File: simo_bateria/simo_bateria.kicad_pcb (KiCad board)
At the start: 2 copper layers, 40.5 x 90 mm, 7 parts, among them J1 Conn_01x02_Male, J2 Conn_01x02_Male, U1 conversor_dc_1_1

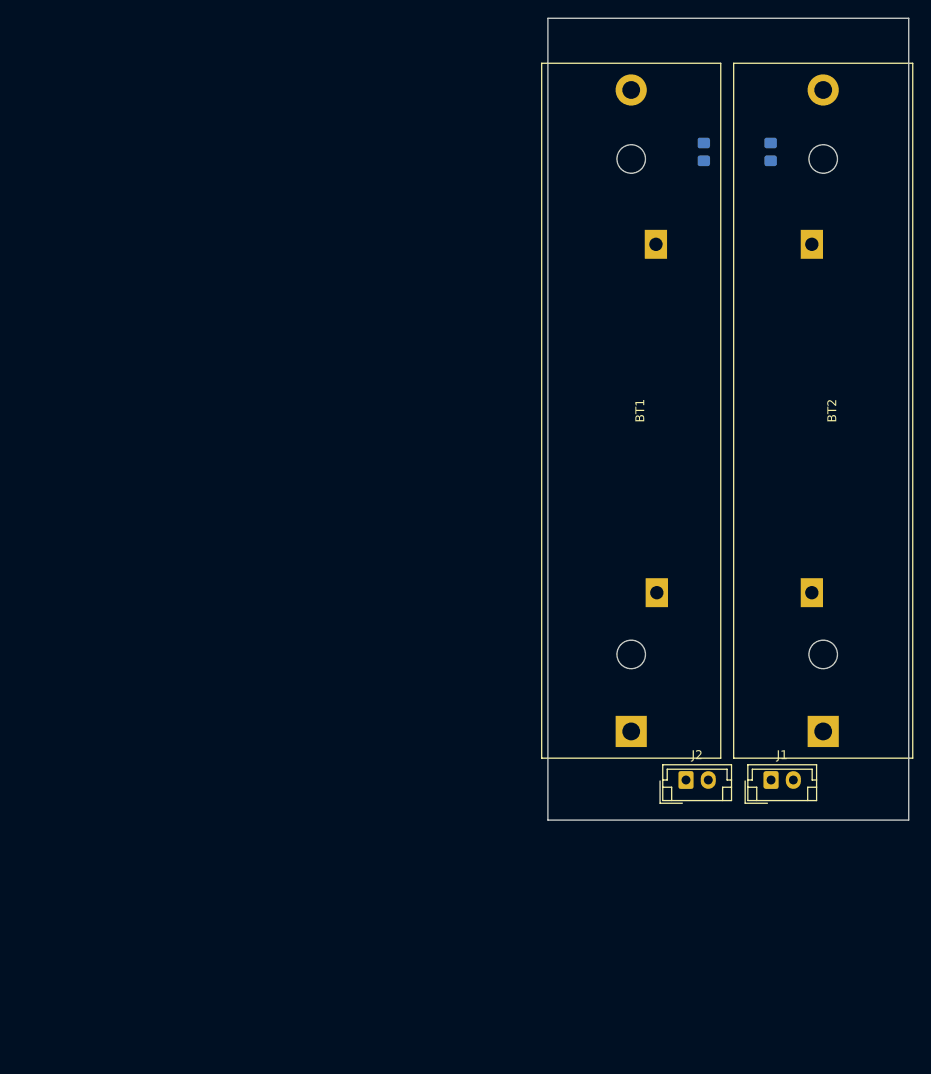
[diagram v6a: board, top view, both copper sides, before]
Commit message: update: placa bateria, correccion de error en esquematico:GND de la salida LEVEL
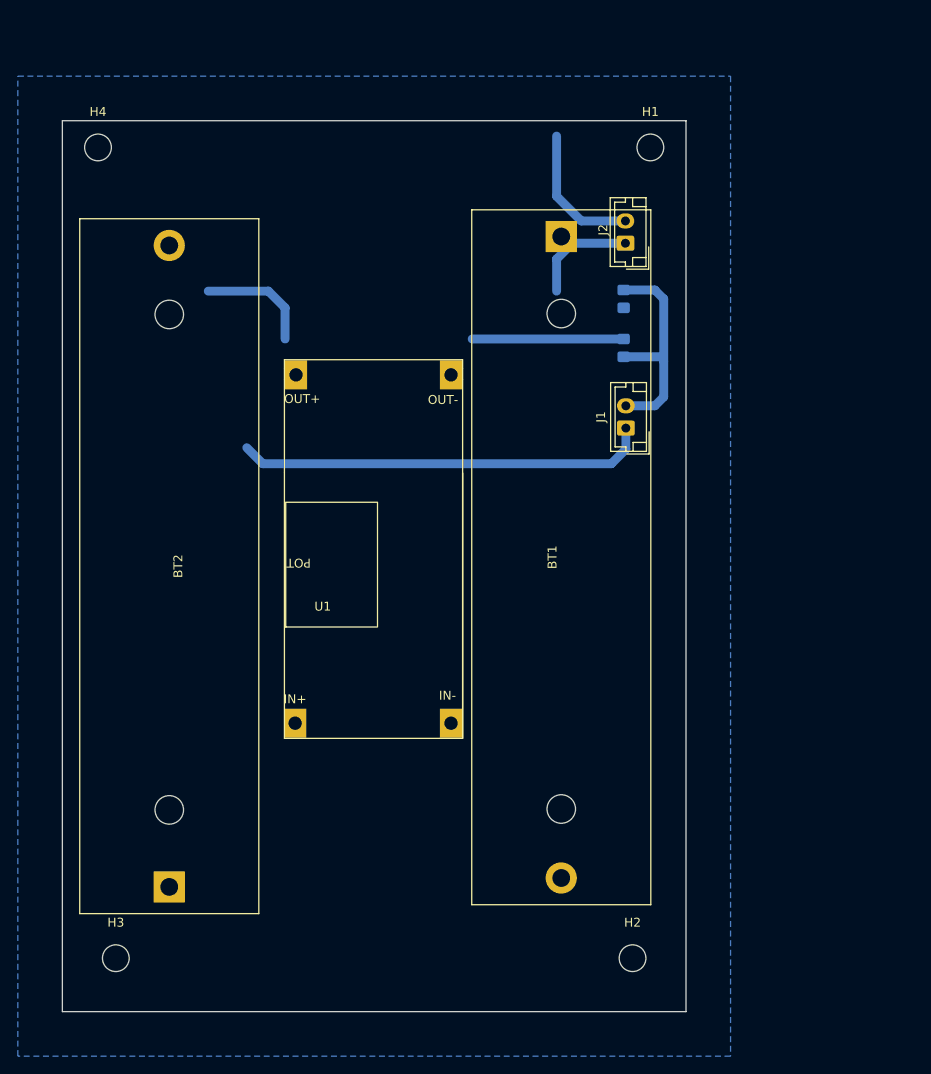
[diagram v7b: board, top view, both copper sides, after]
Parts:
- added H1: MountingHole, MountingHole:MountingHole_3mm, F.Cu at (116.0, 43.0)
- added H2: MountingHole, MountingHole:MountingHole_3mm, F.Cu at (114.0, 134.0)
- added H3: MountingHole, MountingHole:MountingHole_3mm, F.Cu at (56.0, 134.0)
- added H4: MountingHole, MountingHole:MountingHole_3mm, F.Cu at (54.0, 43.0)
- J1: value Conn_01x02_Male -> BAT_LEVEL
- J2: value Conn_01x02_Male -> Plugin
- U1: moved to F.Cu
- moved BT2 75.4 mm to (62.0, 126.0)
- moved U1 67.3 mm to (93.6, 107.6)
- moved J2 60.6 mm to (113.2, 53.8), turned to 90 degrees
- moved BT1 56.1 mm to (106.0, 53.0), turned to -90 degrees
- moved J1 42.7 mm to (113.2, 74.5), turned to 90 degrees
- moved R1 23.8 mm to (113.0, 65.5)
- moved R2 23.3 mm to (113.0, 60.0), turned to -90 degrees
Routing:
- net Net-(BT2-Pad2): track 0.00 -> 59.2 mm
- net Net-(J1-Pad2): track 0.00 -> 24.6 mm
- net Net-(BT1-Pad1): track 0.00 -> 17.0 mm
- net Net-(J2-Pad2): track 0.00 -> 15.6 mm
- net Net-(J2-Pad1): track 0.00 -> 12.1 mm
- added copper zone on B.Cu, net (none)
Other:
- board size 40.5 x 90 mm -> 70 x 100 mm

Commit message: modificaciones en el esquema simo-bateria
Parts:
- added R3: 10k, Resistor_THT:R_Axial_DIN0309_L9.0mm_D3.2mm_P25.40mm_Horizontal, F.Cu at (153.2, 77.0)
- added SW1: SW_Reed, Resistor_THT:R_Axial_DIN0309_L9.0mm_D3.2mm_P25.40mm_Horizontal, F.Cu at (153.2, 81.7)
- added U2: BSS314PEH6327XTSA1, simo_bateria:TRANS_BSS314PEH6327XTSA1_INF, F.Cu at (206.5, 48.0)
- R1, R2: footprint simo_bateria:R_0805_2012Metric_Pad1.20x1.40mm_HandSolder -> Resistor_THT:R_Axial_DIN0309_L9.0mm_D3.2mm_P25.40mm_Horizontal; moved to F.Cu
- U1: value conversor_dc_1_1 -> mod_mt3608; footprint simo_bateria:conversor_dc_dc -> simo_bateria:mt3608_v2
- moved U1 195.0 mm to (281.3, 54.8), turned to 0 degrees
- moved J1 156.2 mm to (269.2, 66.5), turned to 0 degrees
- moved H3 146.1 mm to (191.6, 79.5)
- moved H4 135.0 mm to (184.0, 79.5)
- moved BT1 131.5 mm to (106.0, 184.5), turned to 90 degrees
- moved H2 90.7 mm to (191.6, 87.0)
- moved H1 81.0 mm to (184.0, 87.0)
- moved J2 73.0 mm to (183.8, 72.5), turned to 0 degrees
- moved BT2 49.6 mm to (106.0, 103.0)
- moved R1 45.4 mm to (153.2, 86.5), turned to 0 degrees
- moved R2 42.1 mm to (153.2, 72.2), turned to 0 degrees
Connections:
- BT2 pad 1: Net-(BT1-Pad2) -> Net-(BT1-Pad1)
- BT2 pad 2: Net-(BT2-Pad2) -> Net-(BT1-Pad2)
- J1 pad 1: Net-(BT2-Pad2) -> GND
- J2 pad 1: Net-(J2-Pad1) -> GND
- R2 pad 2: Net-(BT2-Pad2) -> GND
- U1 pad 1: Net-(BT2-Pad2) -> Net-(U1-Pad1)
- U1 pad 2: Net-(J2-Pad1) -> Net-(BT1-Pad2)
- U1 pad 3: Net-(BT1-Pad1) -> Net-(J2-Pad2)
- U1 pad 4: Net-(J2-Pad2) -> GND
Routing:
- net Net-(BT2-Pad2): track 59.2 -> 0.00 mm
- net Net-(J1-Pad2): track 24.6 -> 0.00 mm
- net Net-(BT1-Pad1): track 17.0 -> 0.00 mm
- net Net-(J2-Pad2): track 15.6 -> 0.00 mm
- net Net-(J2-Pad1): track 12.1 -> 0.00 mm
- removed copper zone on B.Cu, net (none)
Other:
- board size 70 x 100 mm -> 70 x 163.5 mm
